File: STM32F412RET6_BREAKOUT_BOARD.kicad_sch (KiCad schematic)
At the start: 20 parts

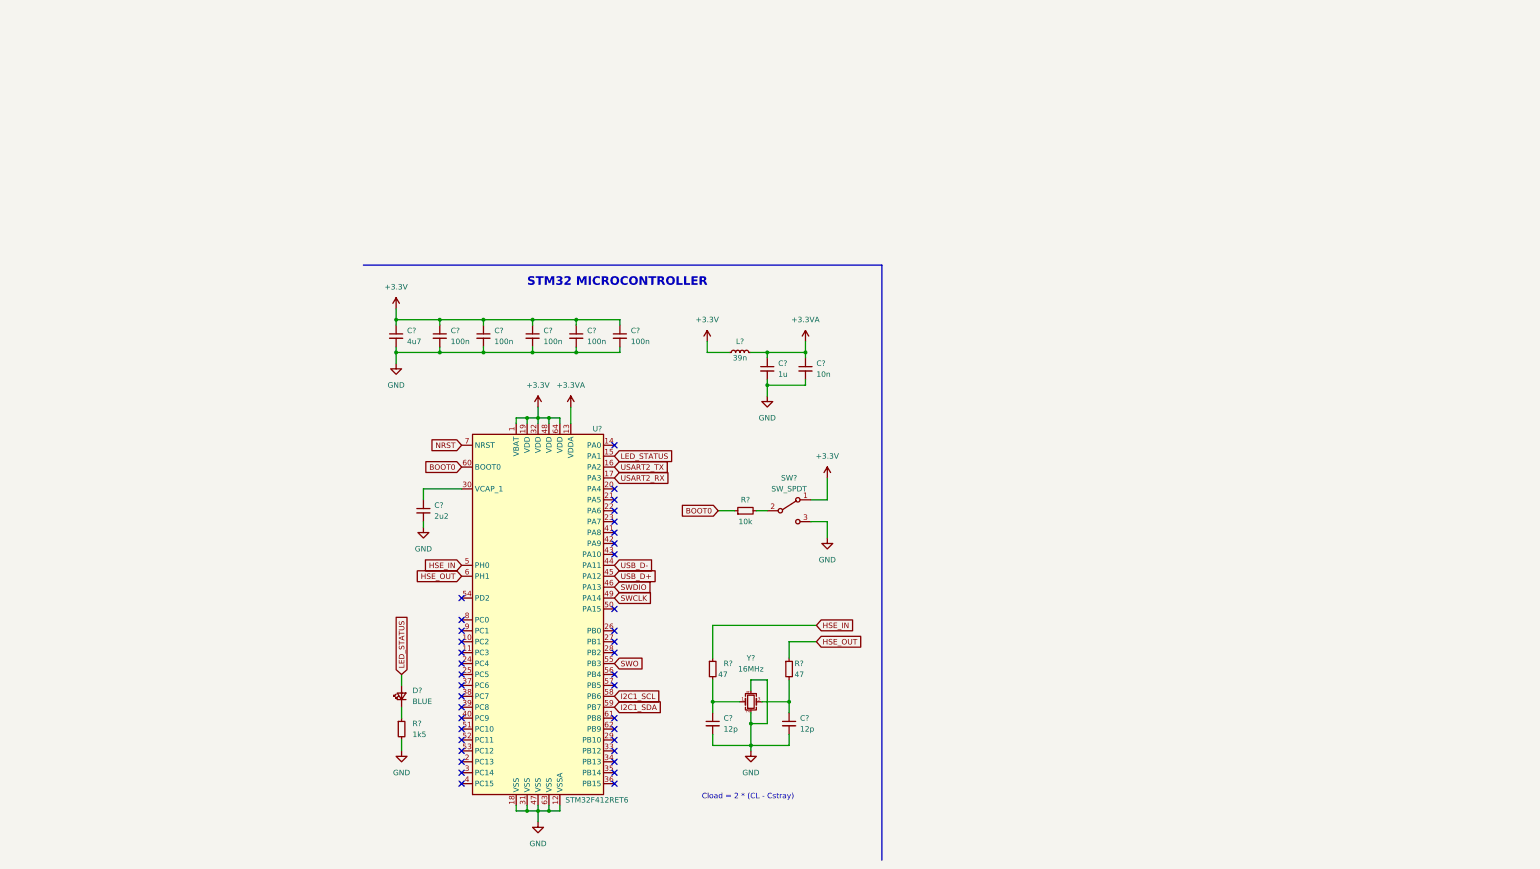
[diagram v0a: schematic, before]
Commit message: Schematic design finish for MCU and Connectors
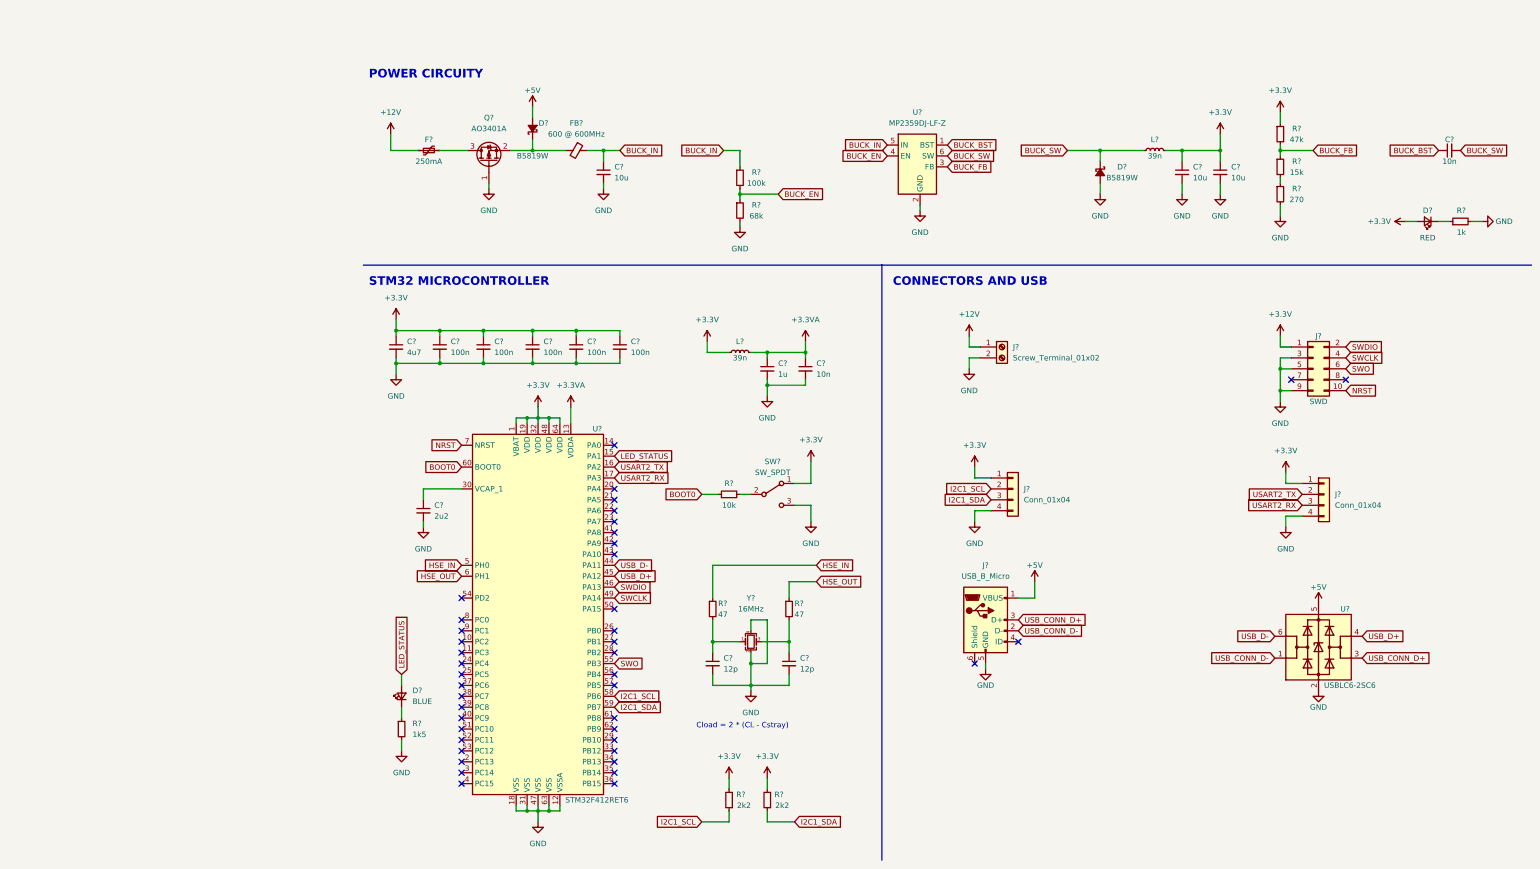
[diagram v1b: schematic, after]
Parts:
- added C?: 10n, symbol Device:C_Small
- added C? (x3): 10u, symbol Device:C_Small
- added D?: RED, symbol Device:LED_Small
- added D? (x2): B5819W, symbol Device:D_Schottky_Small_Filled
- added F?: 250mA, symbol Device:Polyfuse_Small
- added FB?: 600 @ 600MHz, symbol Device:FerriteBead_Small
- added J? (x2): Conn_01x04, symbol Connector_Generic:Conn_01x04
- added J?: SWD, symbol Connector_Generic:Conn_02x05_Odd_Even
- added J?: Screw_Terminal_01x02, symbol Connector:Screw_Terminal_01x02
- added J?: USB_B_Micro, symbol Connector:USB_B_Micro
- added L?: 39n, symbol Device:L_Small
- added Q?: AO3401A, Package_TO_SOT_SMD:SOT-23, symbol Transistor_FET:AO3401A
- added R?: 47k, symbol Device:R_Small
- added R?: 15k, symbol Device:R_Small
- added R?: 1k, symbol Device:R_Small
- added R?: 270, symbol Device:R_Small
- added R? (x2): 2k2, symbol Device:R_Small
- added R?: 68k, symbol Device:R_Small
- added R?: 100k, symbol Device:R_Small
- added U?: USBLC6-2SC6, Package_TO_SOT_SMD:SOT-23-6, symbol Power_Protection:USBLC6-2SC6
- added U?: MP2359DJ-LF-Z, symbol My_Library:MP2359DJ-LF-Z
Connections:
- net +3V3: now also C?.1, C?.1, D?.2 (A), J?.1 (Pin_1), J?.1 (Pin_1), J?.1 (Pin_1), L?.2, R?.1, R?.2, R?.2
- net GND: now also C?.2, C?.2, C?.2, D?.2 (A), J?.2 (Pin_2), J?.3 (Pin_3), J?.4 (Pin_4), J?.4 (Pin_4), J?.5 (GND), J?.5 (Pin_5), J?.9 (Pin_9), Q?.1 (G), R?.2, R?.2, R?.2, U?.2 (GND), U?.2 (GND)
- net I2C1_SCL: now also J?.2 (Pin_2), R?.1
- net I2C1_SDA: now also J?.3 (Pin_3), R?.1
- net NRST: now also J?.10 (Pin_10)
- net SWCLK: now also J?.4 (Pin_4)
- net SWDIO: now also J?.2 (Pin_2)
- net SWO: now also J?.6 (Pin_6)
- net USART2_RX: now also J?.3 (Pin_3)
- net USART2_TX: now also J?.2 (Pin_2)
- net USB_D+: now also U?.4 (I/O2)
- net USB_D-: now also U?.6 (I/O1)
- new net: D?.1 (K), R?.1
- new net: R?.1, R?.2
- new net: D?.1 (K), FB?.2, Q?.2 (S)
- new net: F?.2, Q?.3 (D)
- new net +12V: F?.1, J?.1 (Pin_1)
- new net +5V: D?.2 (A), J?.1 (VBUS), U?.5 (VBUS)
- new net BUCK_BST: C?.1, U?.1 (BST)
- new net BUCK_EN: R?.1, R?.2, U?.4 (EN)
- new net BUCK_FB: R?.1, R?.2, U?.3 (FB)
- new net BUCK_IN: C?.1, FB?.1, R?.1, U?.5 (IN)
- new net BUCK_SW: C?.2, D?.1 (K), L?.1, U?.6 (SW)
- new net USB_CONN_D+: J?.3 (D+), U?.3 (I/O2)
- new net USB_CONN_D-: J?.2 (D-), U?.1 (I/O1)
- no-connect marks 38 -> 42
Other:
- note added: "CONNECTORS AND USB"
- note added: "POWER CIRCUITY"
- moved on the sheet: C?, R?, SW?, Y?

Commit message: add filter for power bus
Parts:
- added C?: 470u, symbol Device:C_Polarized_Small
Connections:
- net +3V3: now also C?.1
- net GND: now also C?.2
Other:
- note added: "CAN BUS PROTOKOLU ICIN BIR CAN MODULU EKLENECEK"
- note added: "CURRENT READING SENSORE EKLENECEK"
- note added: "CURRENT SENSITIVE AKIM OKUMA DEVRESI YAPILACAK"
- note added: "YAPILACAKLAR"
- moved on the sheet: C?, L?, R?, SW?
